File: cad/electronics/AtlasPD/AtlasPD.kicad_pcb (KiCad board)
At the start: 4 copper layers, 150.4 x 115.3 mm, 67 parts, among them J1 Conn_01x02_Male, J2 Conn_01x02_Male, J201 USB_C_Receptacle_USB2.0, J202 Conn_01x04, J301 Conn_01x06, J302 Conn_01x06, J401 Conn_01x04, SW201 SW_SPST, U201 CP2104, U202 ATmega328P-AU, U301 74LS08, U302 DRV8837C, U303 DRV8837C, U401 AMS1117-3.3, U402 LM2678T-ADJ_NOPB, Y201 CSTNE16M0V53-R0

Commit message: Getting Ready to Fab MCU
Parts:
- added REF**: MountingHole_2.2mm_M2_DIN965, MountingHole:MountingHole_2.2mm_M2_DIN965, F.Cu at (216.3, 29.6)
- added REF**: WEEE-Logo_8.4x12mm_SilkScreen, Symbol:WEEE-Logo_8.4x12mm_SilkScreen, B.Cu at (253.4, 56.2)
- moved TP208 5.41 mm to (255.2, 53.1)
- moved TP207 5.41 mm to (255.2, 59.2)
- moved TP209 5.41 mm to (255.2, 51.1)
- moved TP210 5.41 mm to (255.2, 55.1)
- moved TP212 5.41 mm to (255.2, 49.1)
- moved TP211 5.41 mm to (255.2, 57.1)
- moved J202 4.17 mm to (208.4, 53.5)
- moved REF** 2.64 mm to (256.7, 66.0)
- moved REF** 2.64 mm to (256.7, 29.6)
- moved REF** 1.96 mm to (214.2, 59.2)
- moved C201 1.65 mm to (214.7, 39.6)
- moved J201 1.65 mm to (206.3, 36.7)
- moved R201 1.65 mm to (213.1, 36.4)
- moved R202 1.65 mm to (213.1, 33.2)
- moved R203 1.65 mm to (213.1, 39.6)
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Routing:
- net +BATT: track 0.00 -> 35.8 mm, vias 6 -> 12
- net +5V: track 90.8 -> 79.0 mm, vias 19 -> 18
- net /Sheet60A2E58A/RESET: track 43.2 -> 48.7 mm
- net /Motor Driver/EN: track 65.7 -> 69.8 mm
- net GND: track 34.8 -> 38.8 mm, vias 65 -> 69
- net VCC: track 79.6 -> 83.1 mm
- net /Sheet60A2E58A/IO12_MISO: track 7.45 -> 10.8 mm
- net /Motor Driver/IN3: track 37.1 -> 39.4 mm
- net /Motor Driver/PWM_B: track 46.5 -> 48.8 mm
- net /Motor Driver/IN4: track 34.7 -> 36.5 mm
- net /Sheet60A2E58A/USB_DN: track 7.80 -> 6.15 mm
- net /Motor Driver/S4: track 54.5 -> 52.9 mm
- net +3V3: track 13.4 -> 14.9 mm
- net /Sheet60A2E58A/IO1: track 32.1 -> 33.5 mm
- net /Sheet60A2E58A/IO0: track 8.60 -> 9.72 mm
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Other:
- board size 150.4 x 115.3 mm -> 147.8 x 115.3 mm
- rule trace_min: 0.2 -> 0
- board text added: "+BAT"
- board text added: "Atlas MCU Rev. 1.0"

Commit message: Preliminary PCB Production files
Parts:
- removed BT401, BT402: Battery_Cell, Battery:BatteryHolder_Keystone_1042_1x18650
- removed C401: 220uF, Capacitor_THT:CP_Radial_D5.0mm_P2.50mm
- removed C402, C404, C405: 10uF, Capacitor_SMD:C_0805_2012Metric
- removed C406: 1000uF, Capacitor_THT:CP_Radial_D5.0mm_P2.50mm
- removed D401: D_Schottky, Diode_SMD:D_SOD-128
- removed D402: LED, LED_SMD:LED_0805_2012Metric
- removed J1, J2: Conn_01x02_Male, Connector_PinHeader_2.54mm:PinHeader_1x02_P2.54mm_Vertical
- removed J401: Conn_01x04, Connector_JST:JST_PH_B4B-PH-K_1x04_P2.00mm_Vertical
- removed L401: 22 uH, Inductor_SMD:L_TDK_NLV32_3.2x2.5mm
- removed R401: 3.16k, Resistor_SMD:R_0805_2012Metric
- removed R402, R403: 1k, Resistor_SMD:R_0805_2012Metric
- removed the REF** at (253.4, 56.2)
- removed the REF** at (113.9, 108.2)
- removed the REF** at (127.6, 140.2)
- removed U402: LM2678T-ADJ_NOPB, LM2678:TO127P1041X469X2199-7N
- added REF**: ESD-Logo_6.6x6mm_SilkScreen, Symbol:ESD-Logo_6.6x6mm_SilkScreen, B.Cu at (212.3, 64.9)
- added REF**: WEEE-Logo_4.2x6mm_SilkScreen, Symbol:WEEE-Logo_4.2x6mm_SilkScreen, B.Cu at (217.5, 64.9)
- REF**: moved to B.Cu
- moved REF** 34.3 mm to (242.0, 39.1), turned to 180 degrees
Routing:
- net /Sheet60A23886/Output: track 28.4 -> 0.00 mm
- net Net-(BT401-Pad2): track 22.7 -> 0.00 mm
- net Net-(C1-Pad1): track 17.5 -> 0.00 mm
- net Net-(R401-Pad2): track 10.2 -> 0.00 mm
- net Net-(C404-Pad1): track 8.08 -> 0.00 mm
- net Net-(C404-Pad2): track 3.54 -> 0.00 mm
- net Net-(D402-Pad1): track 1.96 -> 0.00 mm
- net +5V: track 79.0 -> 80.4 mm
- net GND: track 38.8 -> 39.3 mm, vias 69 -> 35
- removed copper zone on B.Cu, net GND
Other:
- board size 147.8 x 115.3 mm -> 57.1 x 40.8 mm
- board text removed: "+V"
- board text removed: "Manpreet Singh 2021 DC-DC Converter"
- board text removed: "Output"

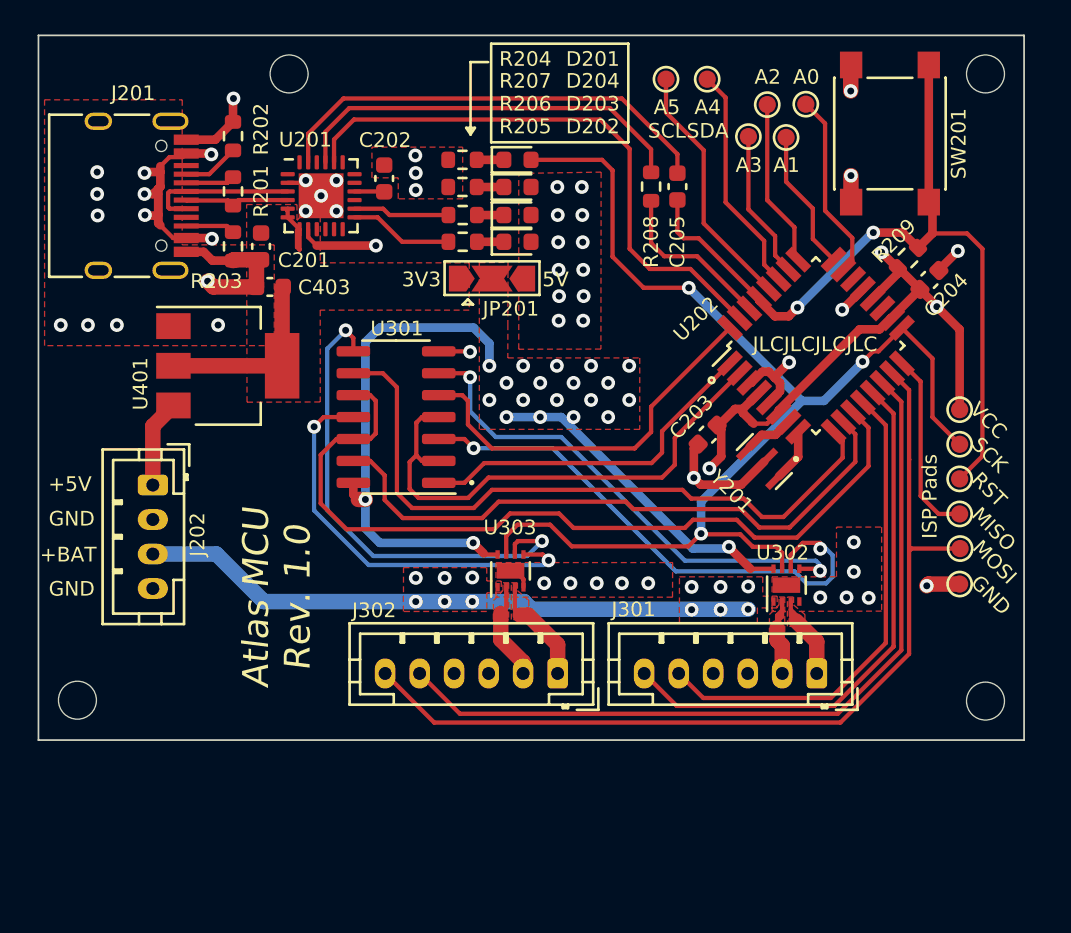
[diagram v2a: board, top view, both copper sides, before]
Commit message: Chaning MCU board size for better layout
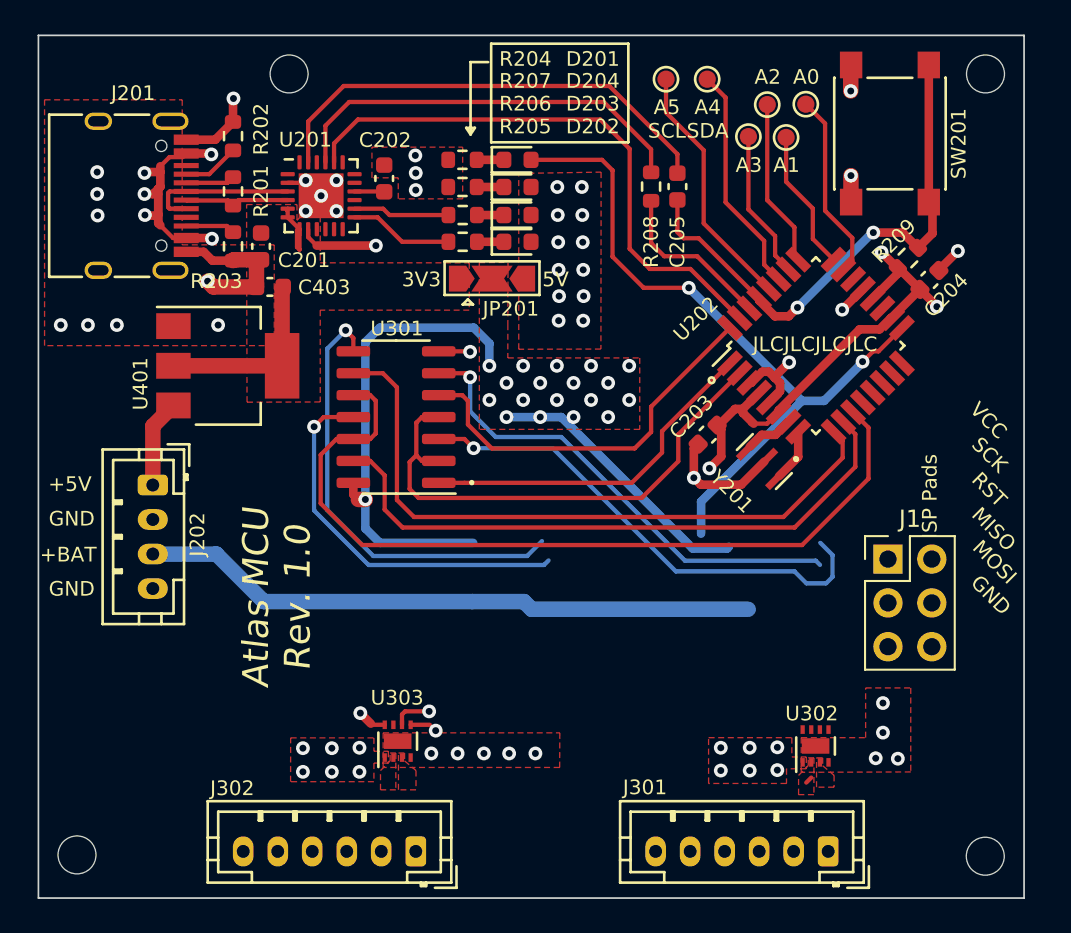
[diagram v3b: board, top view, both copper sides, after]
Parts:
- removed TP207, TP208, TP209, TP210, TP211, TP212: TestPoint_Alt, TestPoint:TestPoint_Pad_D1.0mm
- added J1: Conn_02x03_Odd_Even, Connector_PinHeader_2.54mm:PinHeader_2x03_P2.54mm_Vertical, F.Cu at (251.0, 57.8)
- R204, R207: value R -> 1k
- moved J302 13.2 mm to (223.6, 74.7)
- moved U303 11.8 mm to (222.6, 68.3)
- moved J301 10.3 mm to (247.5, 74.7)
- moved U302 9.47 mm to (246.8, 68.6)
- moved REF** 8.99 mm to (256.7, 75.0)
- moved REF** 8.97 mm to (204.0, 74.9)
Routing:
- net /Motor Driver/S4: track 52.9 -> 0.00 mm
- net /Motor Driver/S3: track 46.4 -> 0.00 mm
- net /Motor Driver/S2: track 31.9 -> 0.00 mm
- net /Motor Driver/S1: track 28.4 -> 0.00 mm
- net /Motor Driver/EN: track 69.8 -> 42.1 mm, vias 3 -> 2
- net /Sheet60A2E58A/RESET: track 48.7 -> 31.6 mm
- net /Sheet60A2E58A/IO12_MISO: track 10.8 -> 0.00 mm
- net VCC: track 83.1 -> 73.3 mm, vias 24 -> 23
- net /Motor Driver/-M2: track 6.29 -> 0.00 mm
- net /Motor Driver/+M2: track 5.66 -> 0.00 mm
- net /Motor Driver/-M1: track 4.88 -> 0.00 mm
- net /Motor Driver/+M1: track 5.19 -> 0.41 mm
- net GND: track 39.3 -> 34.8 mm, vias 35 -> 33
- net /Motor Driver/OUT1: track 31.5 -> 28.7 mm, vias 2 -> 1
- net /Motor Driver/OUT2: track 29.1 -> 27.9 mm, vias 2 -> 1
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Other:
- board size 57.1 x 40.8 mm -> 57.1 x 50 mm

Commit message: New PCB Layout
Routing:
- net /Motor Driver/S4: track 0.00 -> 66.4 mm
- net /Motor Driver/S3: track 0.00 -> 54.6 mm, vias 0 -> 1
- net /Motor Driver/S1: track 0.00 -> 45.1 mm, vias 0 -> 1
- net /Motor Driver/EN: track 42.1 -> 86.7 mm, vias 2 -> 3
- net /Motor Driver/S2: track 0.00 -> 44.6 mm, vias 0 -> 1
- net +BATT: track 35.8 -> 0.00 mm
- net VCC: track 73.3 -> 104.6 mm
- net /Sheet60A2E58A/RESET: track 31.6 -> 62.4 mm
- net /Sheet60A2E58A/IO12_MISO: track 0.00 -> 13.1 mm
- net +5V: track 80.4 -> 88.2 mm
- net /Motor Driver/OUT2: track 27.9 -> 34.8 mm, vias 1 -> 2
- net /Motor Driver/-M2: track 0.00 -> 4.29 mm
- net /Motor Driver/-M1: track 0.00 -> 4.26 mm
- net /Motor Driver/+M2: track 0.00 -> 4.15 mm
- net /Motor Driver/+M1: track 0.41 -> 4.29 mm
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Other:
- board text added: "E1 E2 GND +5V +M -M"
- board text added: "ICSP"
- board text removed: "ISP Pads"

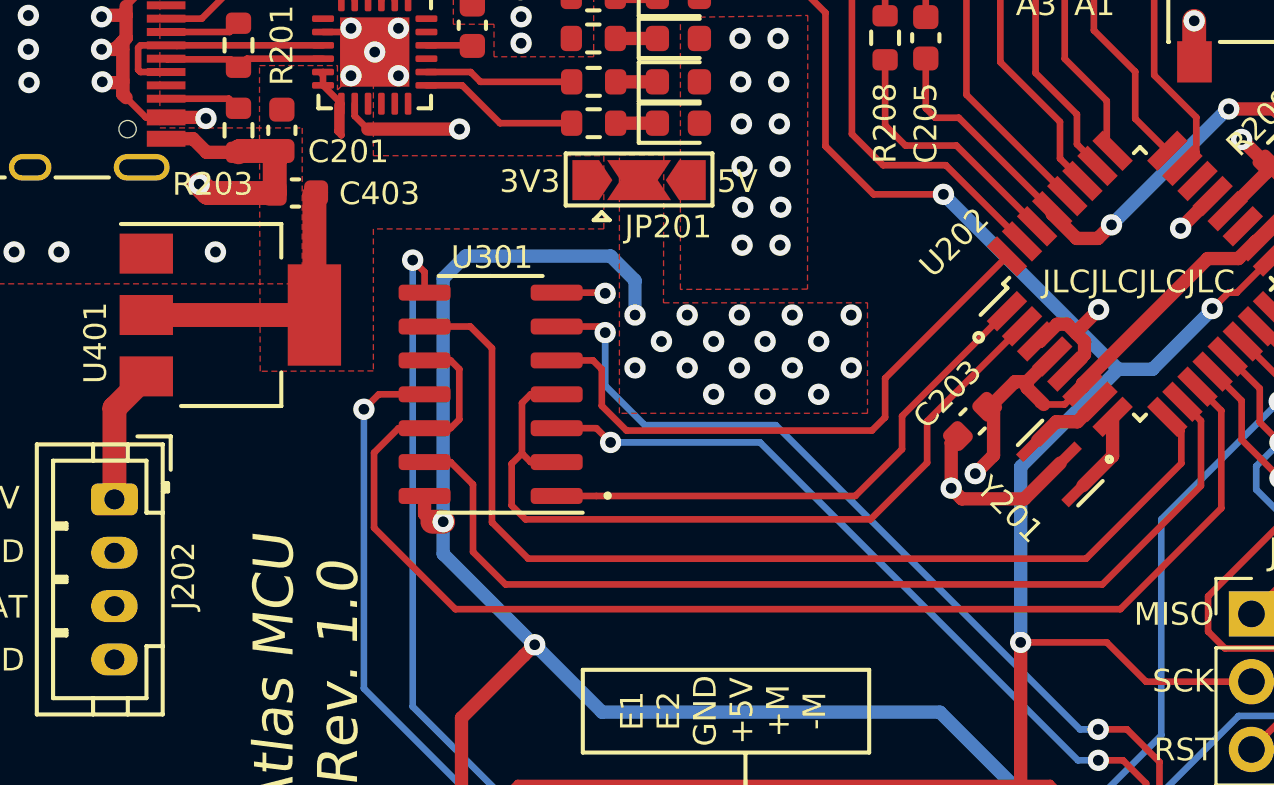
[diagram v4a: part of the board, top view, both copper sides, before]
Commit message: KiCad 6.0 upgrade
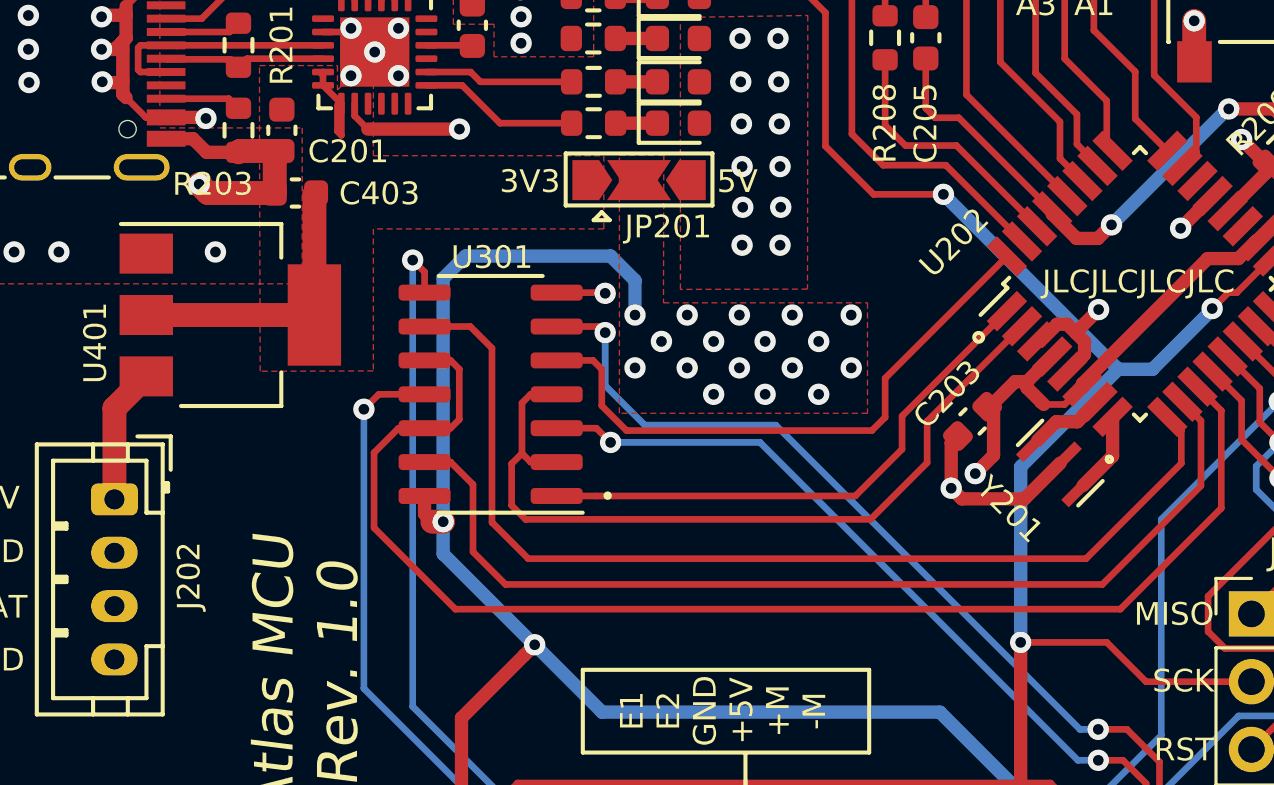
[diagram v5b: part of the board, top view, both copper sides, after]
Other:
- net class Default removed

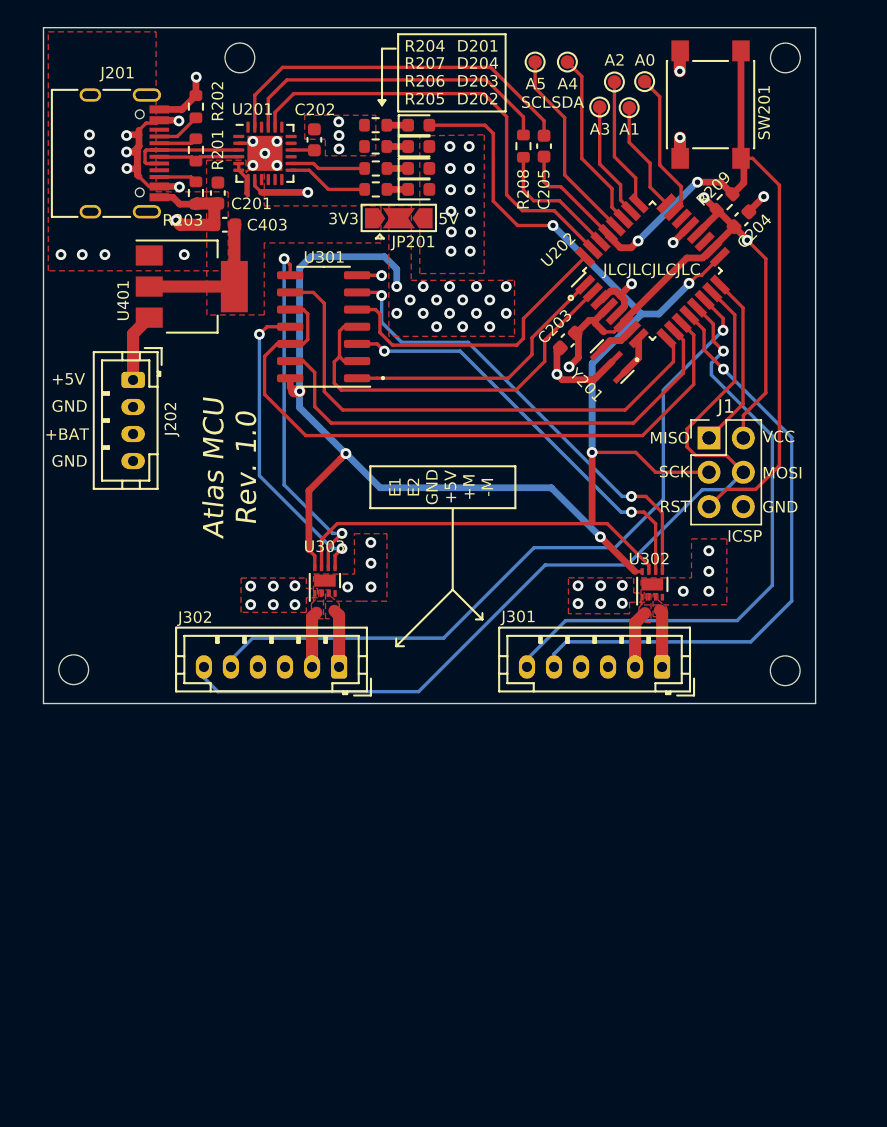
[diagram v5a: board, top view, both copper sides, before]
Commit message: Changing MCU design due to chip shortage affecting current design/plans
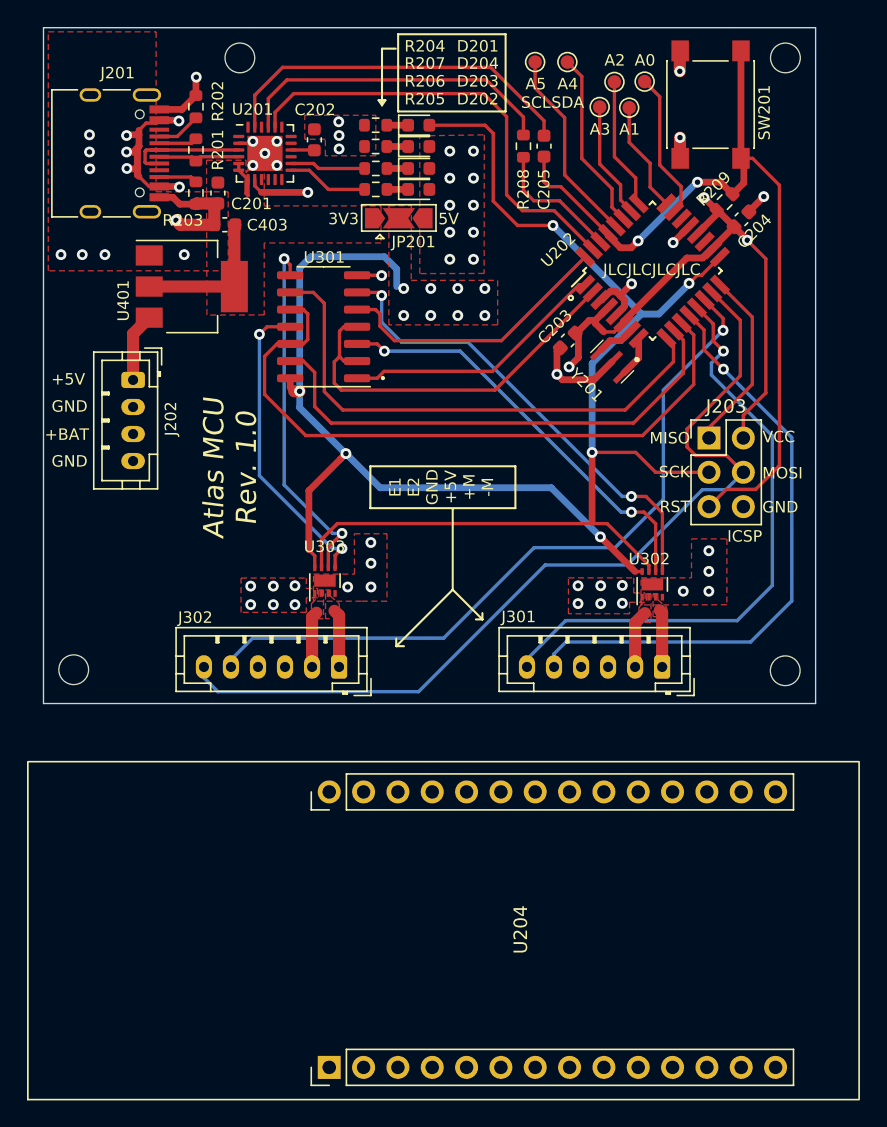
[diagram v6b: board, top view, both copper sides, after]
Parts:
- added U204: Arduino_MKR_Zero, SamacSys_Parts:Arduino MKR Zero, F.Cu at (239.4, 94.1)
- Y201: value CSTNE16M0V53-R0 -> 16MHz
- renumbered J1 to J203
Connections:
- net /Motor Driver/EN renamed /Sheet60A2E58A/IO13_SCK
- net /Motor Driver/IN1 renamed /Sheet60A2E58A/IO2
- net /Motor Driver/IN2 renamed /Sheet60A2E58A/IO3
- net /Motor Driver/IN3 renamed /Sheet60A2E58A/IO5
- net /Motor Driver/IN4 renamed /Sheet60A2E58A/IO6
- net /Motor Driver/PWM_A renamed /Sheet60A2E58A/IO4
- net /Motor Driver/PWM_B renamed /Sheet60A2E58A/IO7
- net /Motor Driver/S1 renamed /Sheet60A2E58A/IO8
- net /Motor Driver/S2 renamed /Sheet60A2E58A/IO9
- net /Motor Driver/S3 renamed /Sheet60A2E58A/IO10_SS
- net /Motor Driver/S4 renamed /Sheet60A2E58A/IO11_MOSI
- J201 pad A8: Net-(J201-PadA8) -> unconnected-(J201-PadA8)
- J201 pad B8: Net-(J201-PadB8) -> unconnected-(J201-PadB8)
- J201 pad S1: Net-(J201-PadS1) -> unconnected-(J201-PadS1)
- U201 pad 1: Net-(U201-Pad1) -> unconnected-(U201-Pad1)
- U201 pad 10: Net-(U201-Pad10) -> unconnected-(U201-Pad10)
- U201 pad 11: Net-(U201-Pad11) -> unconnected-(U201-Pad11)
- U201 pad 12: Net-(U201-Pad12) -> unconnected-(U201-Pad12)
- U201 pad 15: Net-(U201-Pad15) -> unconnected-(U201-Pad15)
- U201 pad 17: Net-(U201-Pad17) -> unconnected-(U201-Pad17)
- U201 pad 18: Net-(U201-Pad18) -> unconnected-(U201-Pad18)
- U201 pad 19: Net-(U201-Pad19) -> unconnected-(U201-Pad19)
- U201 pad 22: Net-(U201-Pad22) -> unconnected-(U201-Pad22)
- U201 pad 24: Net-(U201-Pad24) -> unconnected-(U201-Pad24)
- U201 pad 9: Net-(U201-Pad9) -> unconnected-(U201-Pad9)
- U202 pad 19: Net-(U202-Pad19) -> unconnected-(U202-Pad19)
- U202 pad 22: Net-(U202-Pad22) -> unconnected-(U202-Pad22)
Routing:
- net /Sheet60A2E58A/IO2: track 22.3 -> 20.9 mm
- net /Sheet60A2E58A/IO4: track 30.1 -> 29.2 mm
- net /Sheet60A2E58A/IO3: track 20.5 -> 19.7 mm
- net /Sheet60A2E58A/IO12_MISO: track 13.1 -> 13.7 mm
- net VCC: vias 23 -> 14
- net +5V: vias 18 -> 16
